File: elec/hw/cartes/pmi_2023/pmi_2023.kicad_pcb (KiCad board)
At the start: 2 copper layers, 85 x 100 mm, 277 parts, among them J1 con_servo, J10 Conn_01x01_Pin, J11 Conn_01x01_Socket, J12 Conn_01x01_Pin, J13 Conn_01x01_Pin, J14 Conn_01x01_Socket, J15 Conn_01x01_Socket, J16 Conn_01x01_Pin, J17 Conn_01x01_Pin, J18 Conn_01x01_Pin, J19 Conn_01x01_Pin, J2 con_servo, J20 Conn_01x01_Socket, J21 Conn_01x01_Socket, J22 Conn_01x01_Socket, J23 Conn_01x01_Pin, J24 Conn_01x01_Pin, J25 Conn_01x01_Pin, J26 Conn_01x01_Pin, J27 Conn_01x01_Socket, J28 Conn_01x01_Socket, J29 Conn_01x01_Socket, J3 con_servo, J30 Conn_01x01_Socket, J31 Conn_01x01_Pin, J32 Conn_01x01_Pin, J33 Conn_01x01_Socket, J34 Conn_01x01_Socket, J35 Conn_01x01_Pin, J36 Conn_01x01_Socket, J37 Conn_01x01_Pin, J38 Conn_01x01_Socket, J39 Conn_01x01_Pin, J4 con_servo, J40 Conn_01x01_Pin, J41 Conn_01x01_Socket, J42 Conn_01x01_Socket, J43 Conn_01x01_Socket, J44 Conn_01x01_Pin, J45 Conn_01x01_Socket, J46 Conn_01x01_Pin, J5 254, J7 USB4105-GF-A-060, J8 254, J9 Conn_01x01_Socket, Q2 2N7002, Q3 DMP2008UFG-7, SW1 ESE22MH22, SW2 ESE22MH24, SW5 DS1040-04RN, SW6 2425755-1, SW7 MSS12C02LS-BB2.0, SW8 MSS12C02LS-BB2.0, U1 DRV8231ADDAR, U10 tof_sensor_master, U11 XRA1200PIG16TR-F, U12 LSM6DSO32XTR, U13 GP2S60B, U14 GP2S60B, U15 GP2S60B, U16 GP2S60B, U17 tof_sensor_master, U19 GP2S60B, U2 DRV8231ADDAR, U20 GP2S60B, U21 tof_sensor_master, U23 PCA9685PW, U24 SN74LVC1T45DBV, U25 SN74LVC1T45DBV, U26 SN74LVC1T45DBV, U27 SN74LVC1T45DBV, U28 TLV61070A, U29 TLV61070A, U3 EESX1321, U32 ESP32-S3-WROOM-1, U33 TLV61070A, U34 TLV61070A, U35 LDL1117S33R, U4 EESX1321, U5 AD8531ARTZ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

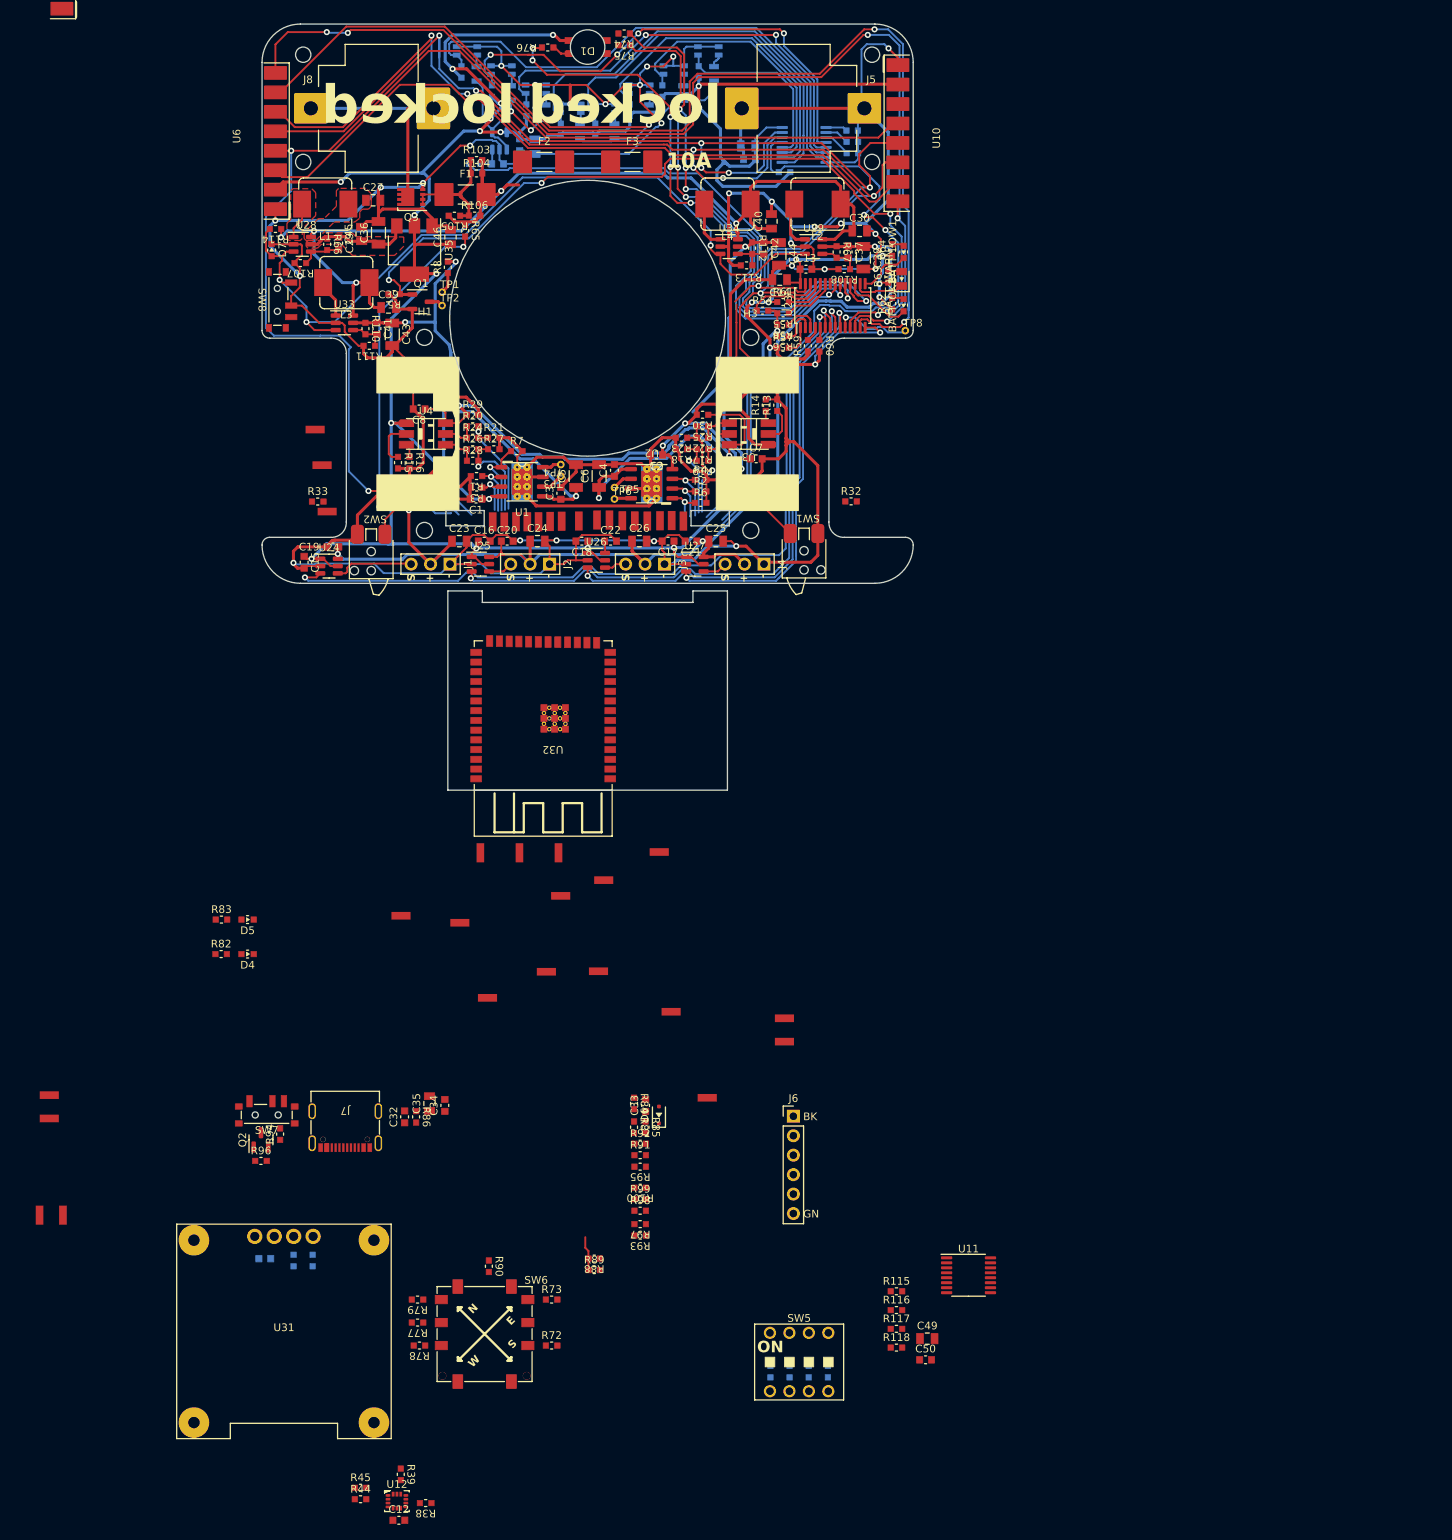
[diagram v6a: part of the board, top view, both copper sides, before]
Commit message: pmi2023: second board components placed
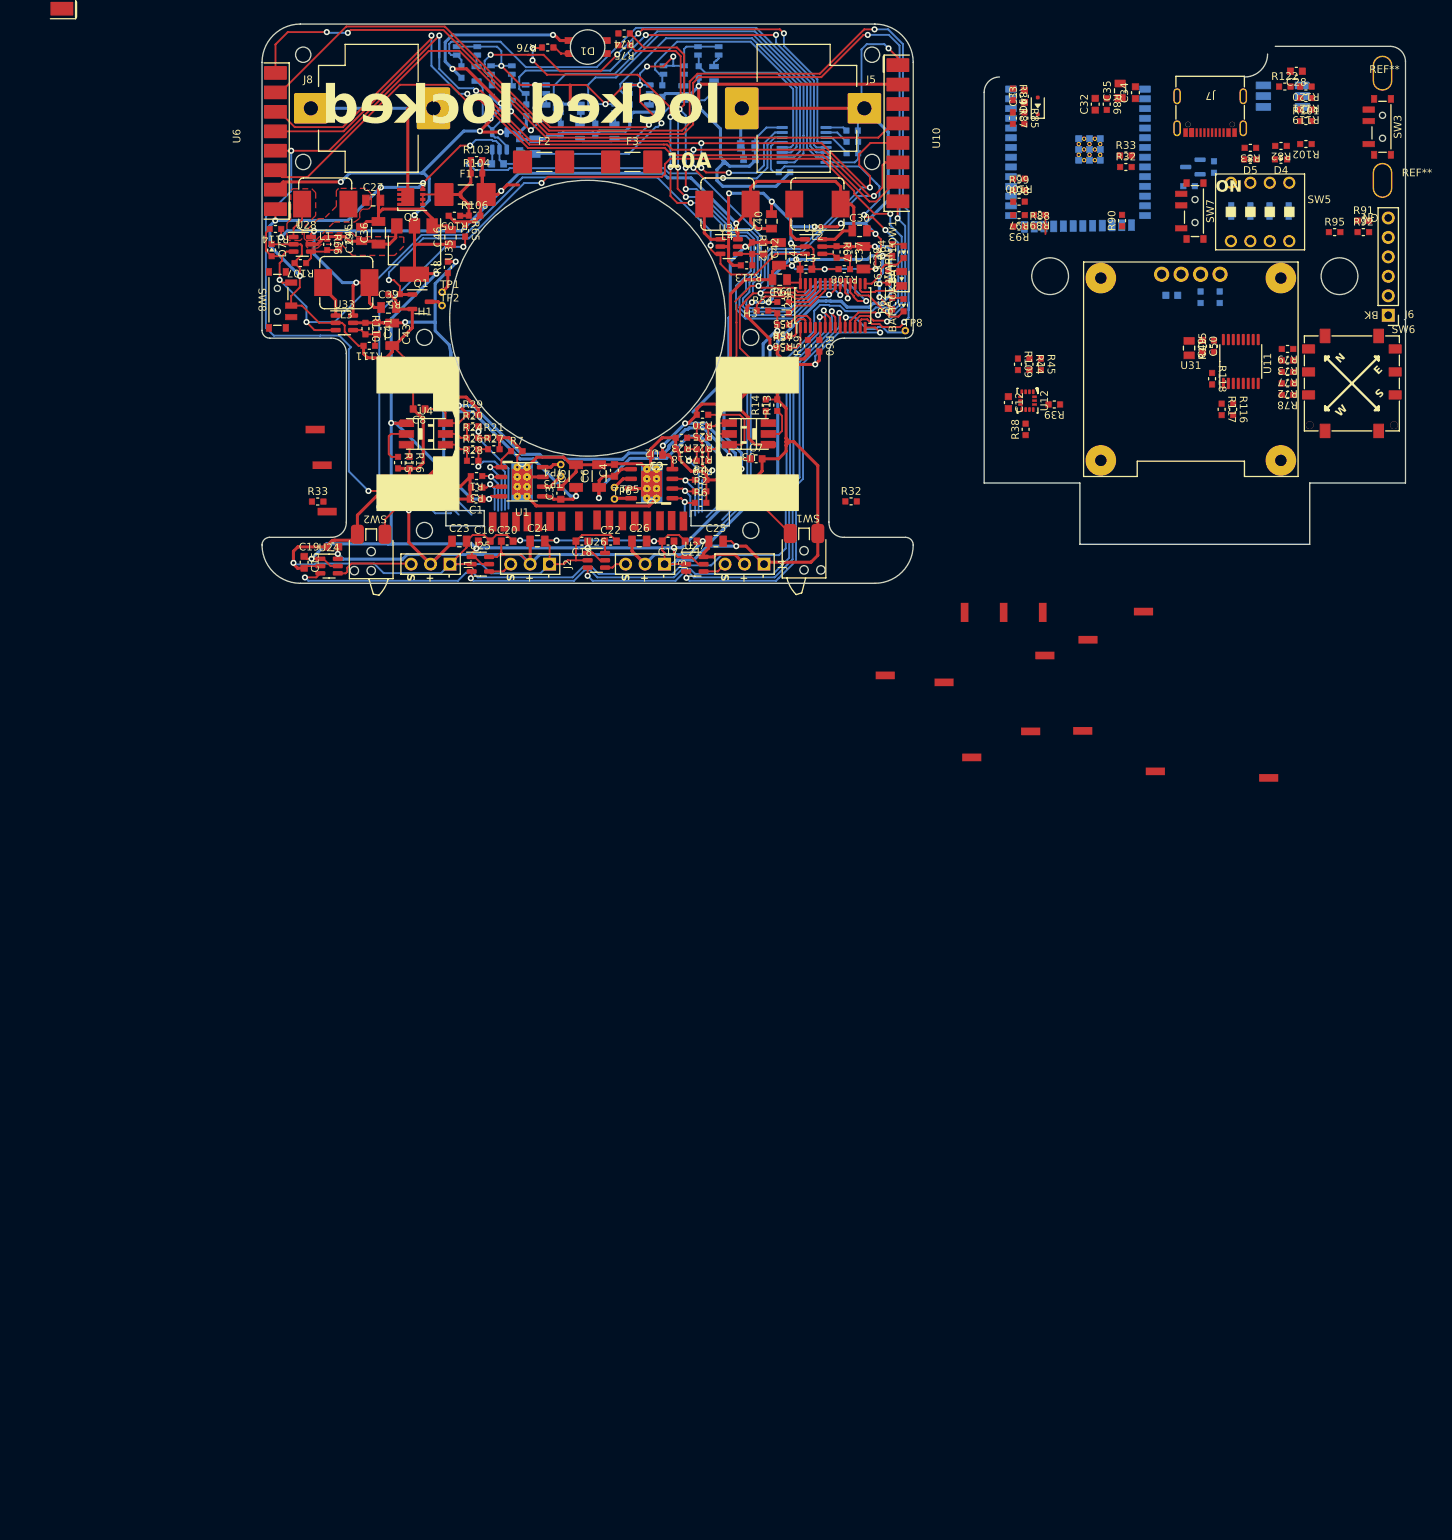
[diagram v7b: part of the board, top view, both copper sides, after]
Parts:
- removed J18, J25, J26, J32, J39, J40: Conn_01x01_Pin, cocotter_others:board_to_module_small
- added C28: 100nF 50V, cocotter_capacitors:C_0603_1608Metric, F.Cu at (235.0, 86.2)
- added R101: 100k, cocotter_resistor:r0603_reflow, F.Cu at (236.3, 92.7)
- added R102: 0R, cocotter_resistor:r0603_reflow, F.Cu at (236.3, 95.7)
- added R109: 0R, cocotter_resistor:r0603_reflow, F.Cu at (198.7, 124.4)
- added R119: 100k, cocotter_resistor:r0603_reflow, F.Cu at (236.3, 91.2)
- added R120: 1k 1%, cocotter_resistor:r0603_reflow, F.Cu at (236.3, 88.2)
- added R121: 1k 1%, cocotter_resistor:r0603_reflow, F.Cu at (236.3, 89.7)
- added R122: 100k, cocotter_resistor:r0603_reflow, F.Cu at (233.5, 88.2)
- added R32: 100k, cocotter_resistor:r0603_reflow, F.Cu at (212.8, 98.7)
- added R33: 100k, cocotter_resistor:r0603_reflow, F.Cu at (212.8, 97.2)
- added REF**: oblong_2mmx3.5mm, cocotter_others:oblong_2mmx3.5mm, F.Cu at (246.5, 86.4)
- added REF**: oblong_2mmx3.5mm, cocotter_others:oblong_2mmx3.5mm, F.Cu at (246.3, 99.9)
- added SW3: MSS12C02LS-BB2.0, cocotter_connectors:MSS12C02LS-BB2.0, F.Cu at (246.3, 93.4)
- added U18: EESX1321, cocotter_ic:EESX1321, B.Cu at (233.3, 89.4)
- Q2, R94, R96, U32: moved to B.Cu
- moved R96 179.7 mm to (224.3, 98.7), turned to -90 degrees
- moved Q2 175.9 mm to (221.5, 98.7), turned to 180 degrees
- moved J7 174.1 mm to (223.8, 86.8)
- moved R82 174.0 mm to (233.0, 95.9), turned to 180 degrees
- moved C31 172.7 mm to (218.8, 115.4)
- moved R80 172.7 mm to (222.5, 115.7)
- moved R81 172.7 mm to (225.0, 115.7)
- moved U31 172.6 mm to (221.2, 125.1)
- moved R44 172.0 mm to (200.2, 124.4), turned to -90 degrees
- moved R45 171.4 mm to (201.7, 124.4), turned to -90 degrees
- moved R94 171.4 mm to (221.0, 101.2), turned to 180 degrees
- moved D4 170.2 mm to (233.0, 97.7)
- moved SW7 169.1 mm to (221.8, 104.4), turned to 90 degrees
- moved R77 168.2 mm to (233.9, 125.4)
- moved R79 168.2 mm to (233.9, 122.4)
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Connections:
- net /boards interface/scl_3v3 renamed /actuators/scl_3v3
- net /boards interface/sda_3v3 renamed /actuators/sda_3v3
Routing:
- net Net-(U32-IO45,GPIO45): track 4.47 -> 2.50 mm
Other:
- board size 85 x 100 mm -> 149.3 x 73 mm
